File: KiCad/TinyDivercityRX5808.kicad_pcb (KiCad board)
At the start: 2 copper layers, 37.4 x 23.7 mm, 23 parts, among them J1 Googles, SW1 SW_DPST, U1 MAX4624/5, U2 ATTINY85-20SU

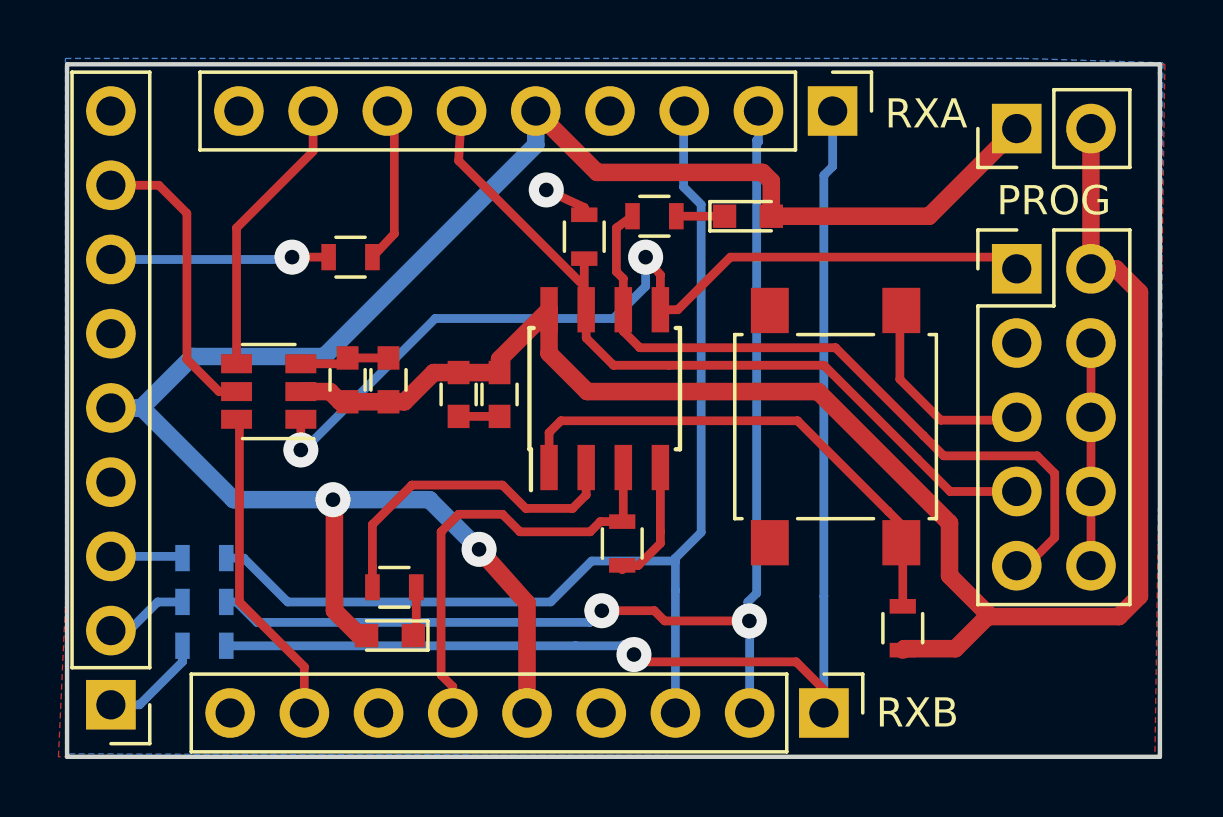
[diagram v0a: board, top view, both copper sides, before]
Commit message: Reworked PCB with larger gaps
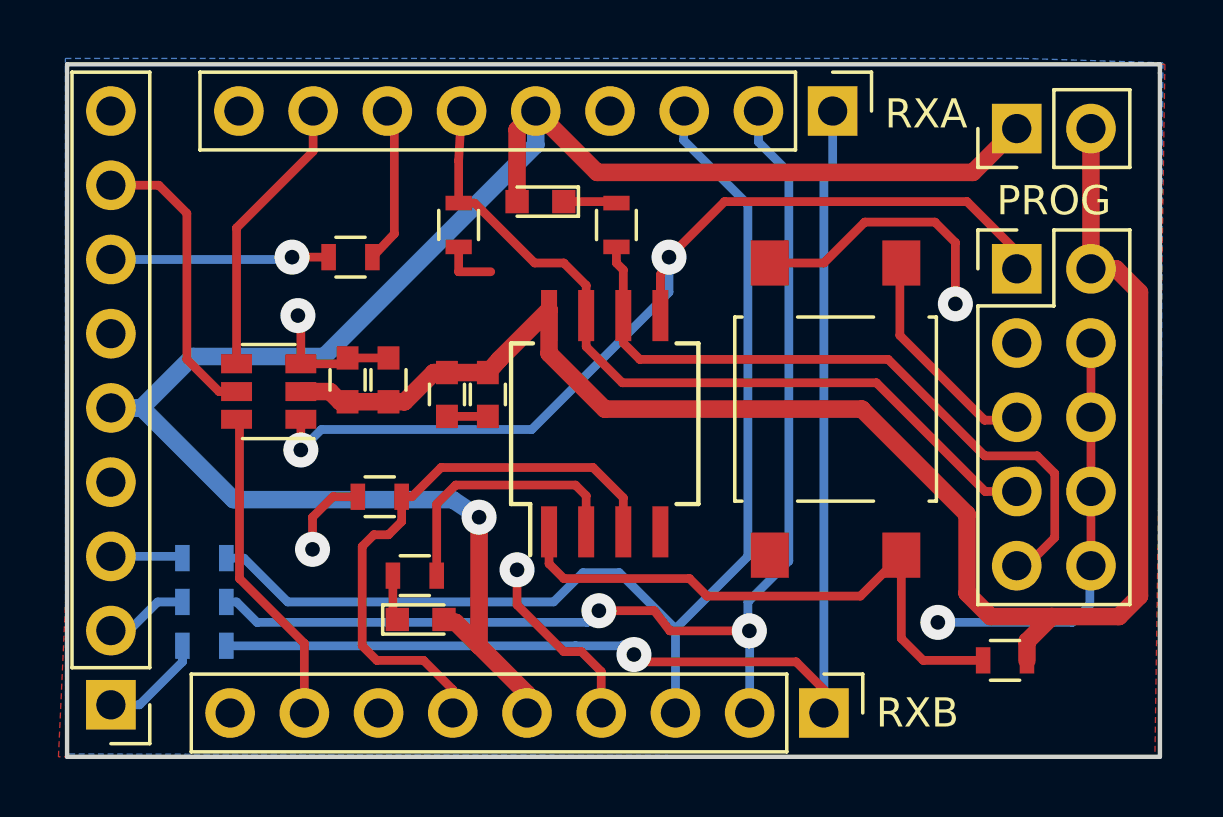
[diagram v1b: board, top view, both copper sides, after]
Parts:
- U2: footprint Housings_SOIC:SOIC-8_3.9x4.9mm_Pitch1.27mm -> Housings_SOIC:SO-8_5.3x6.2mm_Pitch1.27mm
- moved R5 8.45 mm to (138.0, 105.2), turned to 0 degrees
- moved D2 7.12 mm to (143.5, 95.2), turned to 180 degrees
- moved R4 4.32 mm to (140.7, 96.0), turned to 90 degrees
- moved R9 3.67 mm to (159.4, 110.8), turned to 0 degrees
- moved R8 1.33 mm to (146.1, 96.0), turned to 90 degrees
- moved U2 1.20 mm to (145.7, 102.8)
- moved D1 1.19 mm to (139.4, 109.5), turned to 0 degrees
- moved R6 0.81 mm to (139.2, 108.0), turned to 180 degrees
- moved SW1 0.60 mm to (153.6, 102.2)
- moved C4 0.40 mm to (141.7, 101.8)
- moved C1 0.40 mm to (140.3, 101.8)
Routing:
- net GND: track 18.1 -> 41.5 mm, vias 1 -> 5
- net /RSSI_B: track 15.1 -> 20.1 mm
- net /RST: track 25.0 -> 27.9 mm
- net /MOSI: track 31.5 -> 34.0 mm
- net Net-(R6-Pad1): track 11.5 -> 9.22 mm
- net Net-(J2-Pad3): track 39.0 -> 40.9 mm
- net VCC: track 65.7 -> 63.7 mm, vias 2 -> 1
- net Net-(C1-Pad1): track 57.9 -> 56.6 mm
- net Net-(J2-Pad2): track 41.3 -> 42.2 mm
- net /RSSI_A: track 28.7 -> 27.9 mm
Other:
- rule pad_to_mask_clearance: 0.1 -> 0.15
